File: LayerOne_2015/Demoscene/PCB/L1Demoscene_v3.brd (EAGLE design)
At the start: 50 x 50 mm, 40 parts, among them IC2 REG1117, J1 CON_HEADER_1X02-PTH, J2 CON_HEADER_1X02-PTH, J3 CON_HEADER_2X04-PTH, U2 PIC24FXXXDAX06

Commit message: Added Crystal and removed USBID switch
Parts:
- removed LED1: (no value), SparkFun-LED:LED-0603
- removed R4: 750, SparkFun-Resistors:0603-RES
- removed S1: (no value), SparkFun-Electromechanical:SWITCH-SPST-SMD-A
- added C6, C7: 9pF, SparkFun-Capacitors:0603-CAP
- added Y1: (no value), SparkFun-FreqCtrl:CRYSTAL-SMD-5X3
- moved C1 6.65 mm to (14.0, 32.8), turned to 90 degrees
- moved C9 4.58 mm to (2.29, 21.8)
- moved U3 4.57 mm to (2.03, 28.4)
- moved S3 1.52 mm to (1.52, 42.4)
- moved R2 1.30 mm to (2.29, 9.65)
- moved R3 1.05 mm to (2.29, 7.87)
- moved C2 0.51 mm to (3.05, 5.08)
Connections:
- removed net BOOT: LED1.C, U2.39
- new net N$20: C6.1, U2.40, Y1.3
- net 3.3V: no longer R4.2
- net GND: now also C6.2, C7.2; no longer S1.1
- net N$3: now also C7.1, U2.39, Y1.1; no longer LED1.A, R4.1
- net USBID: no longer S1.2
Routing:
- net 3.3V: track 137.8 -> 147.8 mm
- net N$3: track 2.07 -> 10.3 mm
- net N$20: track 0.00 -> 6.73 mm
- net BOOT: track 4.95 -> 0.00 mm
- net D-: track 15.3 -> 18.9 mm
- net D+: track 15.1 -> 18.7 mm
- net VBUS: track 33.3 -> 30.7 mm
- net VIN: track 6.88 -> 8.10 mm
- net USBID: track 22.9 -> 22.1 mm, vias 3 -> 2
- net N$7: track 7.50 -> 6.87 mm

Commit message: Small modifications
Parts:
- C6, C7: value 9pF -> 18pF
- moved C2 0.51 mm to (3.05, 5.59)
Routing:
- net PGED1: track 32.2 -> 33.1 mm
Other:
- board text added: "MCLR"
- board text added: "PGEC1"
- board text added: "PGED1"
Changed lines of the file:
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@@
 <text x="19.558" y="46.736" size="0.8128" layer="25" rot="R90">GND</text>
 <text x="33.782" y="46.736" size="0.8128" layer="25" rot="R90">GND</text>
+<text x="4.572" y="3.556" size="0.4064" layer="25">PGEC1</text>
+<text x="7.112" y="3.556" size="0.4064" layer="25">PGED1</text>
+<text x="9.906" y="3.556" size="0.4064" layer="25">GND</text>
+<text x="12.7" y="3.556" size="0.4064" layer="25">3.3V</text>
+<text x="14.986" y="3.556" size="0.4064" layer="25">MCLR</text>
 </plain>
 <attributes>
@@
 <attribute name="VALUE" x="4.064" y="7.366" size="0.4064" layer="27" font="vector"/>
 </element>
-<element name="C2" library="SparkFun-Capacitors" package="EIA3216" value="10uF" x="3.048" y="5.08" smashed="yes">
-<attribute name="NAME" x="5.842" y="5.334" size="0.4064" layer="25"/>
-<attribute name="VALUE" x="5.842" y="4.572" size="0.4064" layer="27"/>
+<element name="C2" library="SparkFun-Capacitors" package="EIA3216" value="10uF" x="3.048" y="5.588" smashed="yes">
+<attribute name="NAME" x="5.842" y="5.842" size="0.4064" layer="25"/>
+<attribute name="VALUE" x="5.842" y="5.08" size="0.4064" layer="27"/>
 </element>
 <element name="S3" library="SparkFun-Electromechanical" package="SWITCH-SPST-SMD-A" value="" x="1.524" y="42.418" smashed="yes" rot="R90">
@@
 <attribute name="VALUE" x="-0.254" y="18.288" size="0.4064" layer="27" rot="R270"/>
 </element>
-<element name="C6" library="SparkFun-Capacitors" package="0603-CAP" value="9pF" x="2.286" y="11.684" smashed="yes" rot="R180">
+<element name="C6" library="SparkFun-Capacitors" package="0603-CAP" value="18pF" x="2.286" y="11.684" smashed="yes" rot="R180">
 <attribute name="NAME" x="4.064" y="11.684" size="0.4064" layer="25" font="vector"/>
 <attribute name="VALUE" x="4.064" y="11.176" size="0.4064" layer="27" font="vector"/>
 </element>
-<element name="C7" library="SparkFun-Capacitors" package="0603-CAP" value="9pF" x="2.286" y="19.812" smashed="yes">
+<element name="C7" library="SparkFun-Capacitors" package="0603-CAP" value="18pF" x="2.286" y="19.812" smashed="yes">
 <attribute name="NAME" x="4.064" y="20.066" size="0.4064" layer="25" font="vector"/>
 <attribute name="VALUE" x="4.064" y="19.558" size="0.4064" layer="27" font="vector"/>
@@
 <wire x1="12.704" y1="6.608" x2="12.446" y2="6.35" width="0.254" layer="1"/>
 <wire x1="12.446" y1="6.35" x2="7.112" y2="6.35" width="0.254" layer="1"/>
-<wire x1="7.112" y1="6.35" x2="5.842" y2="5.08" width="0.254" layer="1"/>
-<wire x1="5.842" y1="5.08" x2="4.448" y2="5.08" width="0.254" layer="1"/>
+<wire x1="7.112" y1="6.35" x2="6.35" y2="5.588" width="0.254" layer="1"/>
+<wire x1="6.35" y1="5.588" x2="4.448" y2="5.588" width="0.254" layer="1"/>
 </signal>
 <signal name="MCLR">
@@
 <wire x1="4.318" y1="3.302" x2="3.048" y2="4.572" width="0.254" layer="16"/>
 <wire x1="3.048" y1="4.572" x2="3.048" y2="6.604" width="0.254" layer="16"/>
-<wire x1="1.436" y1="7.874" x2="1.436" y2="7.2" width="0.254" layer="1"/>
-<wire x1="1.436" y1="7.2" x2="2.032" y2="6.604" width="0.254" layer="1"/>
-<wire x1="2.032" y1="6.604" x2="3.048" y2="6.604" width="0.254" layer="1"/>
+<wire x1="2.794" y1="6.858" x2="3.048" y2="6.604" width="0.254" layer="1"/>
+<wire x1="2.794" y1="6.858" x2="1.778" y2="6.858" width="0.254" layer="1"/>
+<wire x1="1.778" y1="6.858" x2="1.524" y2="7.112" width="0.254" layer="1"/>
+<wire x1="1.524" y1="7.112" x2="1.524" y2="7.786" width="0.254" layer="1"/>
+<wire x1="1.524" y1="7.786" x2="1.436" y2="7.874" width="0.254" layer="1"/>
 </signal>
 <signal name="VIN">
@@
 <wire x1="21.59" y1="19.558" x2="22.86" y2="19.558" width="0.254" layer="1"/>
 <via x="22.86" y="19.558" extent="1-16" drill="0.5"/>
-<wire x1="22.86" y1="19.558" x2="21.59" y2="19.558" width="0.254" layer="16"/>
-<wire x1="21.59" y1="19.558" x2="19.558" y2="17.526" width="0.254" layer="16"/>
-<wire x1="19.558" y1="17.526" x2="19.558" y2="15.494" width="0.254" layer="16"/>
+<wire x1="19.558" y1="18.288" x2="19.558" y2="15.494" width="0.254" layer="16"/>
 <wire x1="19.558" y1="15.494" x2="14.478" y2="10.414" width="0.254" layer="16"/>
 <wire x1="14.478" y1="10.414" x2="14.478" y2="6.858" width="0.254" layer="16"/>
@@
 <wire x1="8.128" y1="1.778" x2="8.128" y2="3.81" width="0.254" layer="1"/>
 <wire x1="8.128" y1="3.81" x2="9.906" y2="5.588" width="0.254" layer="1"/>
+<wire x1="22.86" y1="19.558" x2="22.352" y2="20.066" width="0.254" layer="16"/>
+<wire x1="22.352" y1="20.066" x2="21.336" y2="20.066" width="0.254" layer="16"/>
+<wire x1="21.336" y1="20.066" x2="19.558" y2="18.288" width="0.254" layer="16"/>
 </signal>
 <signal name="PGEC1">
@@
 <contactref element="R7" pad="2"/>
 <wire x1="16.204" y1="18.704" x2="16.204" y2="22.046" width="0.254" layer="1"/>
-<wire x1="16.204" y1="22.046" x2="17.018" y2="22.86" width="0.254" layer="1"/>
-<via x="17.018" y="22.86" extent="1-16" drill="0.5"/>
-<wire x1="17.018" y1="22.86" x2="17.018" y2="31.496" width="0.254" layer="16"/>
-<wire x1="17.018" y1="31.496" x2="18.288" y2="32.766" width="0.254" layer="16"/>
-<via x="18.288" y="32.766" extent="1-16" drill="0.5"/>
+<via x="16.764" y="22.606" extent="1-16" drill="0.5"/>
+<wire x1="17.018" y1="31.496" x2="20.32" y2="34.798" width="0.254" layer="16"/>
+<via x="20.32" y="34.798" extent="1-16" drill="0.5"/>
 <wire x1="23.622" y1="43.014" x2="23.622" y2="45.466" width="0.254" layer="1"/>
-<wire x1="18.288" y1="32.766" x2="22.352" y2="36.83" width="0.254" layer="1"/>
+<wire x1="20.32" y1="34.798" x2="22.352" y2="36.83" width="0.254" layer="1"/>
 <wire x1="22.352" y1="36.83" x2="22.352" y2="41.744" width="0.254" layer="1"/>
 <wire x1="22.352" y1="41.744" x2="23.622" y2="43.014" width="0.254" layer="1"/>
+<wire x1="16.204" y1="22.046" x2="16.764" y2="22.606" width="0.254" layer="1"/>
+<wire x1="17.018" y1="31.496" x2="17.018" y2="22.86" width="0.254" layer="16"/>
+<wire x1="17.018" y1="22.86" x2="16.764" y2="22.606" width="0.254" layer="16"/>
 </signal>
 <signal name="RP6">
@@
 <contactref element="J3" pad="3"/>
 <contactref element="R6" pad="2"/>
-<wire x1="16.704" y1="18.704" x2="16.704" y2="21.022" width="0.254" layer="1"/>
-<wire x1="16.704" y1="21.022" x2="18.288" y2="22.606" width="0.254" layer="1"/>
-<via x="18.288" y="22.606" extent="1-16" drill="0.5"/>
-<wire x1="18.288" y1="22.606" x2="18.288" y2="30.734" width="0.254" layer="16"/>
+<wire x1="16.704" y1="18.704" x2="16.704" y2="21.276" width="0.254" layer="1"/>
+<via x="18.034" y="23.114" extent="1-16" drill="0.5"/>
 <wire x1="18.288" y1="30.734" x2="20.32" y2="32.766" width="0.254" layer="16"/>
 <via x="20.32" y="32.766" extent="1-16" drill="0.5"/>
@@
 <wire x1="20.32" y1="32.766" x2="24.892" y2="37.338" width="0.254" layer="1"/>
 <wire x1="24.892" y1="37.338" x2="24.892" y2="41.744" width="0.254" layer="1"/>
+<wire x1="16.704" y1="21.276" x2="18.034" y2="22.606" width="0.254" layer="1"/>
+<wire x1="18.034" y1="22.606" x2="18.034" y2="23.114" width="0.254" layer="1"/>
+<wire x1="18.288" y1="30.734" x2="18.288" y2="23.368" width="0.254" layer="16"/>
+<wire x1="18.288" y1="23.368" x2="18.034" y2="23.114" width="0.254" layer="16"/>
 </signal>
 <signal name="RP18">

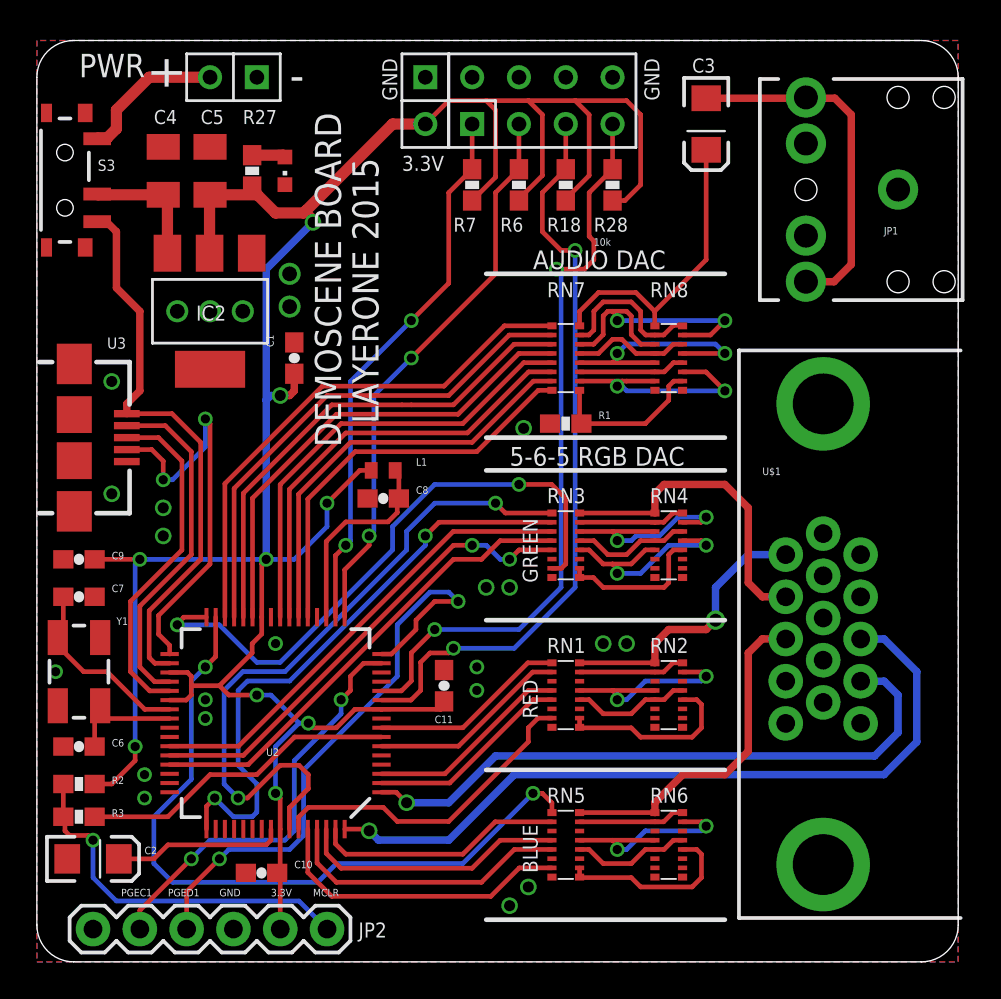
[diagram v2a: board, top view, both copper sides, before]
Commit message: -Set Pins 6,7,8 on the VGA connector to ground for color ground return -Added ground vias for better return paths -Added two extra pads for hackery
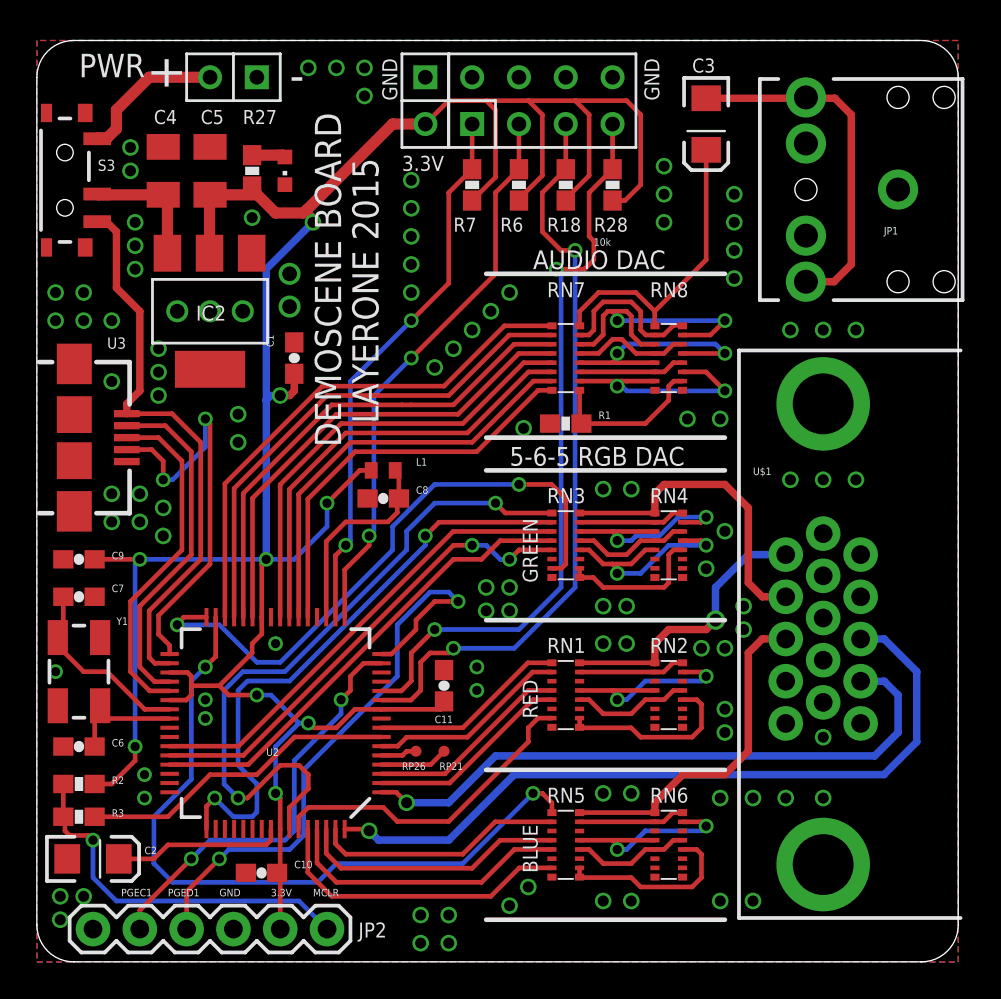
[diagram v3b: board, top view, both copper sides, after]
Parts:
- added RP21, RP26: TPTP06R, testpad:TP06R
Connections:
- new net TP1: RP26.TP, U2.5
- new net TP2: RP21.TP, U2.4
- net GND: now also U$1.6, U$1.7, U$1.8
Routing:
- net TP2: track 0.00 -> 3.69 mm
- net TP1: track 0.00 -> 1.96 mm
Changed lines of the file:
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@@
 <elements>
 <element name="U$1" library="SparkFun-Connectors" package="DB15" value="DB15" x="47.752" y="17.78" smashed="yes" rot="R270">
-<attribute name="NAME" x="39.37" y="26.416" size="0.4064" layer="25" ratio="10"/>
-<attribute name="VALUE" x="39.37" y="25.654" size="0.4064" layer="27" ratio="10"/>
+<attribute name="NAME" x="38.862" y="26.416" size="0.4064" layer="25" ratio="10"/>
+<attribute name="VALUE" x="38.862" y="25.654" size="0.4064" layer="27" ratio="10"/>
 </element>
 <element name="C3" library="SparkFun-Capacitors" package="EIA3216" value="" x="36.322" y="45.466" smashed="yes" rot="R270">
@@
 <attribute name="NAME" x="4.064" y="20.066" size="0.4064" layer="25" font="vector"/>
 <attribute name="VALUE" x="4.064" y="19.558" size="0.4064" layer="27" font="vector"/>
+</element>
+<element name="RP26" library="testpad" package="TP06R" value="TPTP06R" x="20.574" y="11.43" smashed="yes">
+<attribute name="TP_SIGNAL_NAME" value="" x="20.574" y="9.525" size="1" layer="37"/>
+<attribute name="NAME" x="19.812" y="10.414" size="0.4064" layer="25"/>
+</element>
+<element name="RP21" library="testpad" package="TP06R" value="TPTP06R" x="22.098" y="11.43" smashed="yes">
+<attribute name="TP_SIGNAL_NAME" value="" x="22.098" y="9.525" size="1" layer="37"/>
+<attribute name="NAME" x="21.844" y="10.414" size="0.4064" layer="25"/>
 </element>
 </elements>
@@
 <via x="13.716" y="37.338" extent="1-16" drill="0.8"/>
 <via x="13.716" y="35.56" extent="1-16" drill="0.8"/>
+<contactref element="U$1" pad="8"/>
+<contactref element="U$1" pad="7"/>
+<contactref element="U$1" pad="6"/>
+<via x="1.016" y="34.798" extent="1-16" drill="0.6"/>
+<via x="2.54" y="34.798" extent="1-16" drill="0.6"/>
+<via x="4.064" y="34.798" extent="1-16" drill="0.6"/>
+<via x="2.54" y="36.322" extent="1-16" drill="0.6"/>
+<via x="1.016" y="36.322" extent="1-16" drill="0.6"/>
+<via x="5.588" y="25.4" extent="1-16" drill="0.6"/>
+<via x="5.588" y="23.876" extent="1-16" drill="0.6"/>
+<via x="4.064" y="23.876" extent="1-16" drill="0.6"/>
+<via x="10.922" y="28.194" extent="1-16" drill="0.6"/>
+<via x="10.922" y="29.718" extent="1-16" drill="0.6"/>
+<via x="6.604" y="30.734" extent="1-16" drill="0.6"/>
+<via x="6.604" y="32.004" extent="1-16" drill="0.6"/>
+<via x="6.604" y="33.274" extent="1-16" drill="0.6"/>
+<via x="5.334" y="37.592" extent="1-16" drill="0.6"/>
+<via x="5.334" y="38.862" extent="1-16" drill="0.6"/>
+<via x="5.334" y="40.132" extent="1-16" drill="0.6"/>
+<via x="11.684" y="40.386" extent="1-16" drill="0.6"/>
+<via x="21.59" y="32.258" extent="1-16" drill="0.6"/>
+<via x="22.606" y="33.274" extent="1-16" drill="0.6"/>
+<via x="23.622" y="34.29" extent="1-16" drill="0.6"/>
+<via x="24.638" y="35.306" extent="1-16" drill="0.6"/>
+<via x="25.654" y="36.322" extent="1-16" drill="0.6"/>
+<via x="5.08" y="44.196" extent="1-16" drill="0.6"/>
+<via x="5.08" y="42.926" extent="1-16" drill="0.6"/>
+<via x="30.734" y="3.302" extent="1-16" drill="0.6"/>
+<via x="32.258" y="3.302" extent="1-16" drill="0.6"/>
+<via x="37.084" y="3.302" extent="1-16" drill="0.6"/>
+<via x="38.862" y="3.302" extent="1-16" drill="0.6"/>
+<via x="38.862" y="8.89" extent="1-16" drill="0.6"/>
+<via x="37.084" y="8.89" extent="1-16" drill="0.6"/>
+<via x="42.672" y="12.192" extent="1-16" drill="0.6"/>
+<via x="32.258" y="9.144" extent="1-16" drill="0.6"/>
+<via x="30.734" y="9.144" extent="1-16" drill="0.6"/>
+<via x="24.384" y="19.05" extent="1-16" drill="0.6"/>
+<via x="25.654" y="19.05" extent="1-16" drill="0.6"/>
+<via x="30.734" y="19.304" extent="1-16" drill="0.6"/>
+<via x="32.004" y="19.304" extent="1-16" drill="0.6"/>
+<via x="42.672" y="8.89" extent="1-16" drill="0.6"/>
+<via x="34.036" y="40.132" extent="1-16" drill="0.6"/>
+<via x="34.036" y="41.656" extent="1-16" drill="0.6"/>
+<via x="20.32" y="37.846" extent="1-16" drill="0.6"/>
+<via x="30.734" y="25.654" extent="1-16" drill="0.6"/>
+<via x="32.258" y="25.654" extent="1-16" drill="0.6"/>
+<via x="42.672" y="26.162" extent="1-16" drill="0.6"/>
+<via x="44.45" y="26.162" extent="1-16" drill="0.6"/>
+<via x="34.036" y="43.18" extent="1-16" drill="0.6"/>
+<via x="35.306" y="29.464" extent="1-16" drill="0.6"/>
+<via x="37.084" y="29.464" extent="1-16" drill="0.6"/>
+<via x="40.894" y="34.29" extent="1-16" drill="0.6"/>
+<via x="42.672" y="34.29" extent="1-16" drill="0.6"/>
+<via x="44.45" y="34.29" extent="1-16" drill="0.6"/>
+<via x="40.894" y="26.162" extent="1-16" drill="0.6"/>
+<via x="37.846" y="37.084" extent="1-16" drill="0.6"/>
+<via x="37.846" y="38.608" extent="1-16" drill="0.6"/>
+<via x="37.846" y="40.132" extent="1-16" drill="0.6"/>
+<via x="37.846" y="41.656" extent="1-16" drill="0.6"/>
+<via x="36.068" y="17.018" extent="1-16" drill="0.6"/>
+<via x="37.338" y="17.018" extent="1-16" drill="0.6"/>
+<via x="38.354" y="18.034" extent="1-16" drill="0.6"/>
+<via x="38.354" y="19.304" extent="1-16" drill="0.6"/>
+<via x="37.338" y="13.716" extent="1-16" drill="0.6"/>
+<via x="37.338" y="12.446" extent="1-16" drill="0.6"/>
+<via x="40.64" y="8.89" extent="1-16" drill="0.6"/>
+<via x="37.338" y="23.368" extent="1-16" drill="0.6"/>
+<via x="36.322" y="21.336" extent="1-16" drill="0.6"/>
+<via x="20.32" y="36.322" extent="1-16" drill="0.6"/>
+<via x="20.32" y="39.37" extent="1-16" drill="0.6"/>
+<via x="20.32" y="40.894" extent="1-16" drill="0.6"/>
+<via x="20.32" y="42.418" extent="1-16" drill="0.6"/>
+<via x="17.78" y="48.514" extent="1-16" drill="0.6"/>
+<via x="17.78" y="46.99" extent="1-16" drill="0.6"/>
+<via x="16.256" y="48.514" extent="1-16" drill="0.6"/>
+<via x="14.732" y="48.514" extent="1-16" drill="0.6"/>
+<via x="1.27" y="2.286" extent="1-16" drill="0.6"/>
+<via x="1.27" y="3.556" extent="1-16" drill="0.6"/>
+<via x="2.54" y="3.556" extent="1-16" drill="0.6"/>
+<via x="20.828" y="2.54" extent="1-16" drill="0.6"/>
+<via x="22.352" y="2.54" extent="1-16" drill="0.6"/>
+<via x="20.828" y="1.016" extent="1-16" drill="0.6"/>
+<via x="22.352" y="1.016" extent="1-16" drill="0.6"/>
 </signal>
 <signal name="HSYNC">
@@
 <contactref element="U2" pad="2"/>
 <contactref element="RN1" pad="5"/>
+<wire x1="27.952" y1="14.228" x2="26.928" y2="14.228" width="0.254" layer="1"/>
 <wire x1="18.704" y1="9.704" x2="22.404" y2="9.704" width="0.254" layer="1"/>
 <wire x1="22.404" y1="9.704" x2="26.928" y2="14.228" width="0.254" layer="1"/>
-<wire x1="27.952" y1="14.228" x2="26.928" y2="14.228" width="0.254" layer="1"/>
 </signal>
 <signal name="GD13">
 <contactref element="U2" pad="3"/>
 <contactref element="RN1" pad="4"/>
+<wire x1="27.952" y1="14.728" x2="26.666" y2="14.728" width="0.254" layer="1"/>
 <wire x1="18.704" y1="10.204" x2="22.142" y2="10.204" width="0.254" layer="1"/>
 <wire x1="22.142" y1="10.204" x2="26.666" y2="14.728" width="0.254" layer="1"/>
-<wire x1="27.952" y1="14.728" x2="26.666" y2="14.728" width="0.254" layer="1"/>
 </signal>
 <signal name="GD10">
@@
 <contactref element="U2" pad="6"/>
 <contactref element="RN1" pad="2"/>
-<wire x1="18.704" y1="11.704" x2="22.88" y2="11.704" width="0.254" layer="1"/>
-<wire x1="22.88" y1="11.704" x2="26.904" y2="15.728" width="0.254" layer="1"/>
 <wire x1="27.952" y1="15.728" x2="26.904" y2="15.728" width="0.254" layer="1"/>
+<wire x1="18.704" y1="11.704" x2="19.578" y2="11.704" width="0.254" layer="1"/>
+<wire x1="19.578" y1="11.704" x2="20.066" y2="12.192" width="0.254" layer="1"/>
+<wire x1="20.066" y1="12.192" x2="23.368" y2="12.192" width="0.254" layer="1"/>
+<wire x1="23.368" y1="12.192" x2="26.904" y2="15.728" width="0.254" layer="1"/>
 </signal>
 <signal name="GD15">
@@
 <wire x1="1.436" y1="17.898" x2="1.136" y2="17.598" width="0.254" layer="1"/>
 </signal>
+<signal name="TP2">
+<contactref element="U2" pad="4"/>
+<contactref element="RP21" pad="TP"/>
+<wire x1="18.704" y1="10.704" x2="21.372" y2="10.704" width="0.254" layer="1"/>
+<wire x1="21.372" y1="10.704" x2="22.098" y2="11.43" width="0.254" layer="1"/>
+</signal>
+<signal name="TP1">
+<contactref element="U2" pad="5"/>
+<contactref element="RP26" pad="TP"/>
+<wire x1="18.704" y1="11.204" x2="19.84" y2="11.204" width="0.254" layer="1"/>
+<wire x1="19.84" y1="11.204" x2="20.066" y2="11.43" width="0.254" layer="1"/>
+<wire x1="20.066" y1="11.43" x2="20.574" y2="11.43" width="0.254" layer="1"/>
+</signal>
 </signals>
